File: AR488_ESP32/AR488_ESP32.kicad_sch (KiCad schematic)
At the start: 18 parts, among them J1 GPIB_24, J2 DC_7-12V, J3 SHIELD, Q1 AO4407A, U1 Heltec_WiFi_Kit_32_V2, U2 SN75160BDW, U3 SN75161BN, U4 MCP23017, U5 AMS1117-5.0

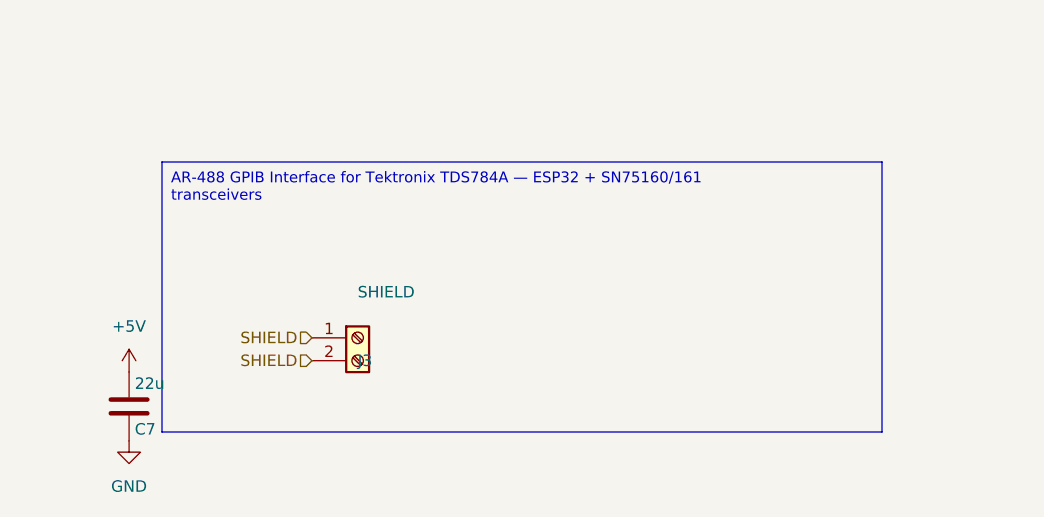
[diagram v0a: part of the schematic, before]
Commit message: feat: v0.3 — remove annotation, force A4, C1 to 0603
- Remove docstring text box annotation from schematic (comments=False)
- Force A4 paper size (components now fit with 3 rows)
- Change C1 (LDO input cap) from 0805 to 0603 package
- Bump revision to 0.3

Co-Authored-By: Claude Opus 4.6 <noreply@anthropic.com>
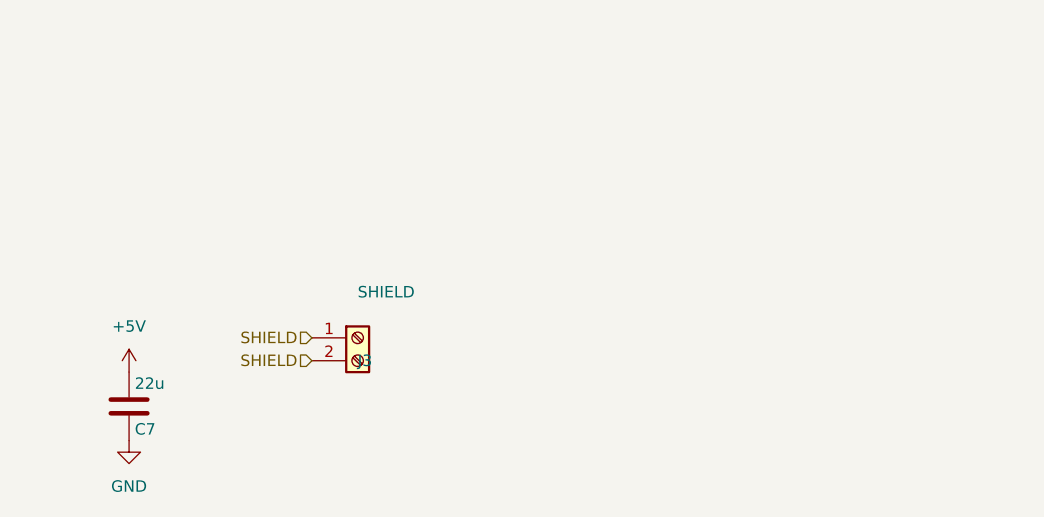
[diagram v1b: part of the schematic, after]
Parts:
- C1: footprint Capacitor_SMD:C_0805_2012Metric -> Capacitor_SMD:C_0603_1608Metric; hierarchy_path /28fd33e5-5818-4e1a-9e9d-00c66b80c42a -> /c3051dcb-604d-4fe0-8085-43f178ab49a3; root_uuid 28fd33e5-5818-4e1a-9e9d-00c66b80c42a -> c3051dcb-604d-4fe0-8085-43f178ab49a3
- C2, C3, C4, C5, C6, C7, D1, J1, J2, J3, Q1, R1, U1, U2, U3, U4, U5: hierarchy_path /28fd33e5-5818-4e1a-9e9d-00c66b80c42a -> /c3051dcb-604d-4fe0-8085-43f178ab49a3; root_uuid 28fd33e5-5818-4e1a-9e9d-00c66b80c42a -> c3051dcb-604d-4fe0-8085-43f178ab49a3

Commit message: docs: v0.4 — rewrite README with project intent, workflow, electrical architecture
Co-Authored-By: Claude Opus 4.6 <noreply@anthropic.com>
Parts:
- C1, C2, C3, C4, C5, C6, C7, D1, J1, J2, J3, Q1, R1, U1, U2, U3, U4, U5: hierarchy_path /c3051dcb-604d-4fe0-8085-43f178ab49a3 -> /9abb8f01-95c2-4415-84b9-c2d85c9cb37e; root_uuid c3051dcb-604d-4fe0-8085-43f178ab49a3 -> 9abb8f01-95c2-4415-84b9-c2d85c9cb37e

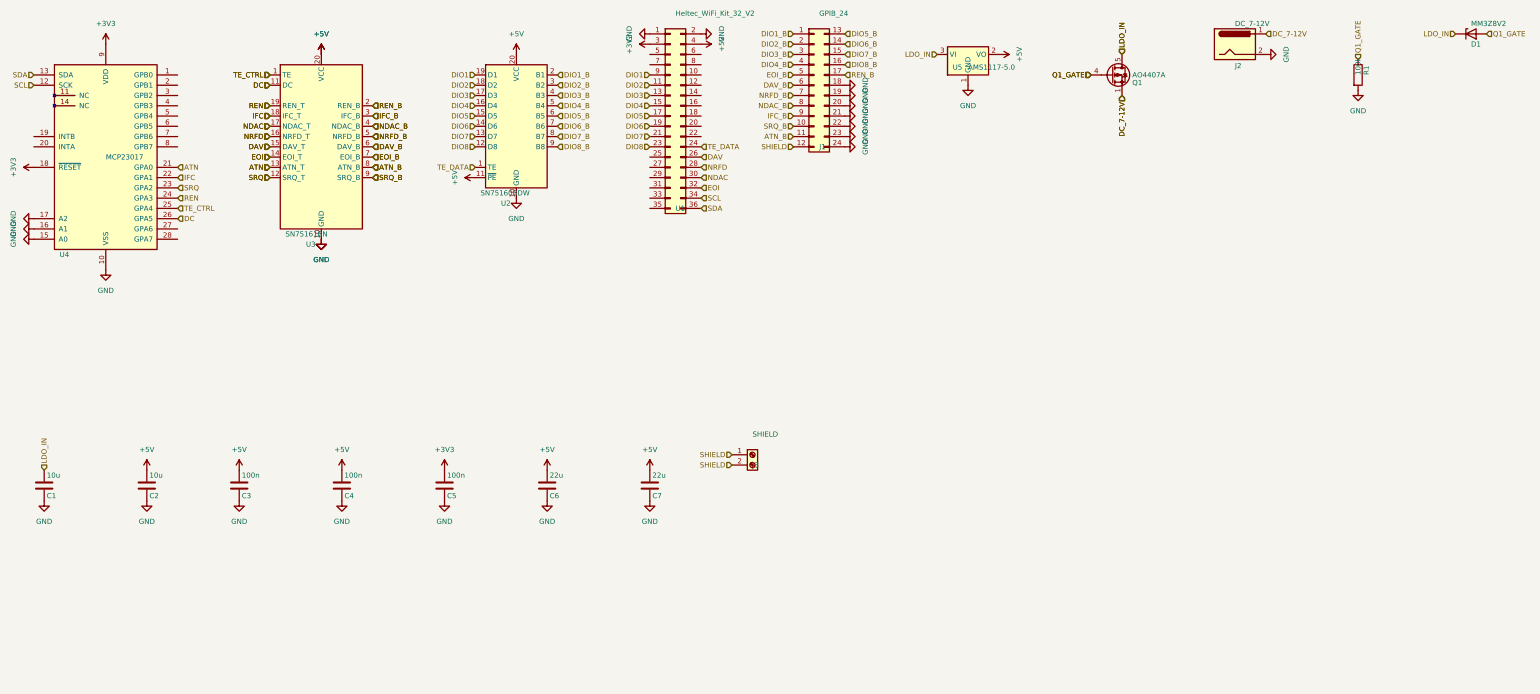
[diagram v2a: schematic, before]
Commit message: feat: v0.5 — switch Q1 to AO3401A, fix ERC to 0 errors
- Replace Q1 AO4407A (SOIC-8) with AO3401A (SOT-23) for simpler RPP
- Convert all hierarchical labels to net labels (fix 30+ ERC errors)
- Add no-connect flags on unused U4 (MCP23017) and U1 (ESP32) pins
- Add PWR_FLAG symbols on +5V, +3V3, GND, LDO_IN nets
- Add solder-friendly Centronics footprint variant (0.6mm drill, 4.2mm row spacing)
- Move custom libs from libs/ to AR488_ESP32/libs/ with fp/sym-lib-table
- Add PCB board file, net classes (Power: 0.6mm track), edge cuts
- Update CLAUDE.md with MCP server guidance and project conventions

Co-Authored-By: Claude Opus 4.6 <noreply@anthropic.com>
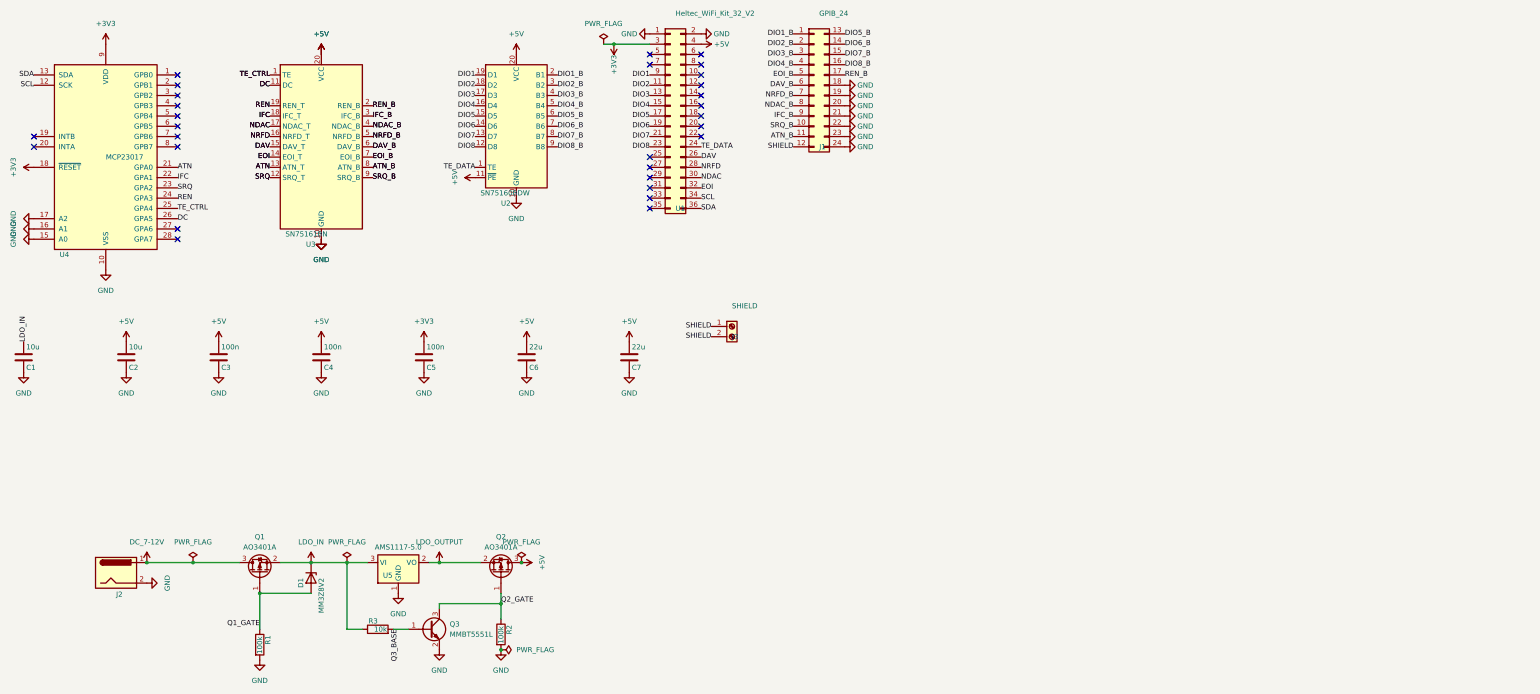
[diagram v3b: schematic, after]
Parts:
- removed Q1: AO4407A, Package_SO:SOIC-8_3.9x4.9mm_P1.27mm, symbol AR488_custom:AO4407A
- added Q1, Q2: AO3401A, Package_TO_SOT_SMD:SOT-23, symbol Transistor_FET:AO3401A
- added Q3: MMBT5551L, Package_TO_SOT_SMD:SOT-23, symbol Transistor_BJT:MMBT5551L
- added R2: 100k, Resistor_SMD:R_0603_1608Metric, symbol Device:R
- added R3: 10k, Resistor_SMD:R_0603_1608Metric, symbol Device:R
- J1: footprint AR488_custom:Centronics_24_GPIB -> AR488_custom:Centronics_24_GPIB_solder
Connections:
- net +5V: now also Q2.3 (D); no longer U5.2 (VO)
- net DC_7-12V: now also Q1.3 (D)
- net GND: now also Q3.2 (E), R2.2
- net LDO_IN: now also Q1.2 (S), R3.1
- net Q1_GATE: now also Q1.1 (G)
- new net LDO_OUTPUT: Q2.2 (S), U5.2 (VO)
- new net Q2_GATE: Q2.1 (G), Q3.3 (C), R2.1
- new net Q3_BASE: Q3.1 (B), R3.2
- no-connect marks 0 -> 29
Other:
- moved on the sheet: C1, C2, C3, C4, C5, C6, C7, D1, J2, J3, R1, U5

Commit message: feat: update GPIB solder footprint — plated oblong mounting holes, 55mm outline
- Mounting holes: plated through-hole oval (3x1mm drill, 3.6x1.6mm pad)
  with pad numbers 25/26 for OUT_SHIELD net connection
- Courtyard width extended from 52.3mm to 55mm
- PCB and schematic updates from KiCad editor (PWR_FLAGs, F8 sync)

Co-Authored-By: Claude Opus 4.6 <noreply@anthropic.com>
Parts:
- C2: value 10u -> 100n
- C6: value 22u -> 1u
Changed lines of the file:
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@@
 			)
 		)
-		(property "Value" "10u"
+		(property "Value" "100n"
 			(at 51.435 102.87 0)
 			(effects
@@
 			)
 		)
-		(property "Value" "22u"
+		(property "Value" "1u"
 			(at 150.495 102.87 0)
 			(effects

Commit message: feat: v1.1 — PCB and schematic updates, Elecrow manufacturing v1.1
Co-Authored-By: Claude Opus 4.6 <noreply@anthropic.com>
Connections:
- net +5V: now also Q2.2 (S), R2.2; no longer Q2.3 (D)
- net GND: no longer R2.2
- net LDO_OUTPUT: now also Q2.3 (D); no longer Q2.2 (S)
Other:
- moved on the sheet: Q2, R2
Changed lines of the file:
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@@
 		(title "AR488_ESP32")
 		(date "2026-04-11")
-		(rev "1.0")
+		(rev "1.1")
 		(comment 1 "AR-488 GPIB Interface for Tektronix TDS784A")
 		(comment 3 "Generated by circuit-synth and modified by author")
@@
 	)
 	(junction
-		(at 143.51 177.8)
-		(diameter 0)
-		(color 0 0 0 0)
-	)
-	(junction
 		(at 105.41 156.21)
 		(diameter 0)
@@
 	)
 	(junction
+		(at 128.27 177.8)
+		(diameter 0)
+		(color 0 0 0 0)
+	)
+	(junction
+		(at 146.05 156.21)
+		(diameter 0)
+		(color 0 0 0 0)
+	)
+	(junction
 		(at 128.27 156.21)
 		(diameter 0)
@@
 	)
 	(junction
-		(at 143.51 166.37)
+		(at 137.16 166.37)
 		(diameter 0)
 		(color 0 0 0 0)
@@
 	(wire
 		(pts
+			(xy 146.05 156.21) (xy 148.59 156.21)
+		)
+		(stroke
+			(width 0)
+			(type default)
+		)
+	)
+	(wire
+		(pts
+			(xy 146.05 156.21) (xy 146.05 157.48)
+		)
+		(stroke
+			(width 0)
+			(type default)
+		)
+	)
+	(wire
+		(pts
+			(xy 142.24 156.21) (xy 146.05 156.21)
+		)
+		(stroke
+			(width 0)
+			(type default)
+		)
+	)
+	(wire
+		(pts
 			(xy 55.88 156.21) (xy 67.31 156.21)
 		)
@@
 	(wire
 		(pts
-			(xy 128.27 156.21) (xy 138.43 156.21)
+			(xy 128.27 156.21) (xy 132.08 156.21)
 		)
 		(stroke
@@
 	(wire
 		(pts
-			(xy 143.51 166.37) (xy 128.27 166.37)
+			(xy 137.16 166.37) (xy 146.05 166.37)
 		)
 		(stroke
@@
 	(wire
 		(pts
-			(xy 143.51 163.83) (xy 143.51 166.37)
+			(xy 137.16 166.37) (xy 128.27 166.37)
 		)
 		(stroke
@@
 	(wire
 		(pts
-			(xy 143.51 166.37) (xy 143.51 170.18)
+			(xy 137.16 163.83) (xy 137.16 166.37)
+		)
+		(stroke
+			(width 0)
+			(type default)
+		)
+	)
+	(wire
+		(pts
+			(xy 146.05 166.37) (xy 146.05 165.1)
 		)
 		(stroke
@@
 	)
 	(label "Q2_GATE"
-		(at 143.51 166.37 0)
+		(at 146.05 166.37 180)
 		(effects
 			(font
 				(size 1.27 1.27)
 			)
-			(justify left bottom)
+			(justify right bottom)
 		)
 	)
@@
 	(symbol
 		(lib_id "power:PWR_FLAG")
-		(at 143.51 177.8 270)
+		(at 128.27 177.8 270)
 		(unit 1)
 		(exclude_from_sim no)
@@
 		(fields_autoplaced yes)
 		(property "Reference" "#FLG03"
-			(at 145.415 177.8 0)
+			(at 130.175 177.8 0)
 			(effects
 				(font
@@
 		)
 		(property "Value" "PWR_FLAG"
-			(at 147.32 177.7999 90)
+			(at 132.08 177.7999 90)
 			(effects
 				(font
@@
 		)
 		(property "Footprint" ""
-			(at 143.51 177.8 0)
+			(at 128.27 177.8 0)
 			(effects
 				(font
@@
 		)
 		(property "Datasheet" "~"
-			(at 143.51 177.8 0)
+			(at 128.27 177.8 0)
 			(effects
 				(font
@@
 		)
 		(property "Description" "Special symbol for telling ERC where power comes from"
-			(at 143.51 177.8 0)
+			(at 128.27 177.8 0)
 			(effects
 				(font
@@
 	(symbol
 		(lib_id "Transistor_FET:AO3401A")
-		(at 143.51 158.75 270)
-		(mirror x)
+		(at 137.16 158.75 90)
 		(unit 1)
 		(exclude_from_sim no)
@@
 		(dnp no)
 		(property "Reference" "Q2"
-			(at 143.51 149.86 90)
+			(at 137.16 149.86 90)
 			(effects
 				(font
@@
 		)
 		(property "Value" "AO3401A"
-			(at 143.51 152.4 90)
+			(at 137.16 152.4 90)
 			(effects
 				(font
@@
 		)
 		(property "Footprint" "Package_TO_SOT_SMD:SOT-23"
-			(at 141.605 153.67 0)
+			(at 139.065 153.67 0)
 			(effects
 				(font
@@
 		)
 		(property "Datasheet" "http://www.aosmd.com/pdfs/datasheet/AO3401A.pdf"
-			(at 139.7 153.67 0)
+			(at 140.97 153.67 0)
 			(effects
 				(font
@@
 		)
 		(property "Description" "-4.0A Id, -30V Vds, P-Channel MOSFET, SOT-23"
-			(at 143.51 158.75 0)
+			(at 137.16 158.75 0)
 			(effects
 				(font
@@
 	(symbol
 		(lib_id "Device:R")
-		(at 143.51 173.99 0)
+		(at 146.05 161.29 180)
 		(unit 1)
 		(exclude_from_sim no)
@@
 		(dnp no)
 		(property "Reference" "R2"
-			(at 145.542 173.99 90)
+			(at 144.018 161.29 90)
 			(effects
 				(font
@@
 		)
 		(property "Value" "100k"
-			(at 143.51 176.276 90)
+			(at 146.05 159.004 90)
 			(effects
 				(font
@@
 		)
 		(property "Footprint" "Resistor_SMD:R_0603_1608Metric"
-			(at 141.732 173.99 90)
+			(at 147.828 161.29 90)
 			(effects
 				(font
@@
 		)
 		(property "Datasheet" ""
-			(at 143.51 173.99 0)
+			(at 146.05 161.29 0)
 			(effects
 				(font
@@
 		)
 		(property "Description" ""
-			(at 143.51 173.99 0)
+			(at 146.05 161.29 0)
 			(effects
 				(font
@@
 		)
 		(property "hierarchy_path" "/9abb8f01-95c2-4415-84b9-c2d85c9cb37e"
-			(at 146.05 179.0699 0)
+			(at 143.51 156.2101 0)
 			(effects
 				(font
@@
 		)
 		(property "project_name" "AR488_ESP32"
-			(at 146.05 179.0699 0)
+			(at 143.51 156.2101 0)
 			(effects
 				(font
@@
 		)
 		(property "root_uuid" "9abb8f01-95c2-4415-84b9-c2d85c9cb37e"
-			(at 146.05 179.0699 0)
+			(at 143.51 156.2101 0)
 			(effects
 				(font
@@
 					(unit 1)
 				)
-			)
-		)
-	)
-	(symbol
-		(lib_id "power:GND")
-		(at 143.51 177.8 0)
-		(unit 1)
-		(exclude_from_sim no)
-		(in_bom yes)
-		(on_board yes)
-		(dnp no)
-		(property "Reference" "#PWR01"
-			(at 143.51 171.45 0)
-			(effects
-				(font
-					(size 1.27 1.27)
-				)
-				(justify left)
-				(hide yes)
-			)
-		)
-		(property "Value" "GND"
-			(at 143.51 182.88 0)
-			(effects
-				(font
-					(size 1.27 1.27)
-				)
-			)
-		)
-		(property "Footprint" ""
-			(at 143.51 177.8 0)
-			(effects
-				(font
-					(size 1.27 1.27)
-				)
-				(hide yes)
-			)
-		)
-		(property "Datasheet" ""
-			(at 143.51 177.8 0)
-			(effects
-				(font
-					(size 1.27 1.27)
-				)
-			)
-		)
-		(property "Description" ""
-			(at 143.51 177.8 0)
-			(effects
-				(font
-					(size 1.27 1.27)
-				)
-			)
-		)
-		(pin "1"
-		)
-		(instances
-			(project "AR488_ESP32"
-				(path "/9abb8f01-95c2-4415-84b9-c2d85c9cb37e"
-					(reference "#PWR01")
-					(unit 1)
-				)
